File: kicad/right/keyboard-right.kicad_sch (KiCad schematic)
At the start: 87 parts, among them J1 Conn_01x04_Pin, J2 AudioJack4, J3 Conn_01x04_Pin, J4 Conn_01x04_Pin, J5 Conn_01x02_Pin, SW1 SW_Push, SW10 SW_Push, SW11 SW_Push, SW12 SW_Push, SW13 SW_Push, SW14 SW_Push, SW15 SW_Push, SW16 SW_Push, SW17 SW_Push, SW18 SW_Push, SW19 SW_Push, SW2 SW_Push, SW20 SW_Push, SW21 SW_Push, SW22 SW_Push, SW23 SW_Push, SW24 SW_Push, SW25 SW_Push, SW26 SW_Push, SW27 SW_Push, SW28 SW_Push, SW29 SW_Push, SW3 SW_Push, SW30 SW_Push, SW31 SW_Push, SW32 SW_Push, SW33 SW_Push, SW34 SW_Push, SW35 SW_Push, SW36 SW_Push, SW4 SW_Push, SW5 SW_Push, SW6 SW_Push, SW7 SW_Push, SW8 SW_Push, SW9 SW_Push, U1 AVR32DA32x-xPT

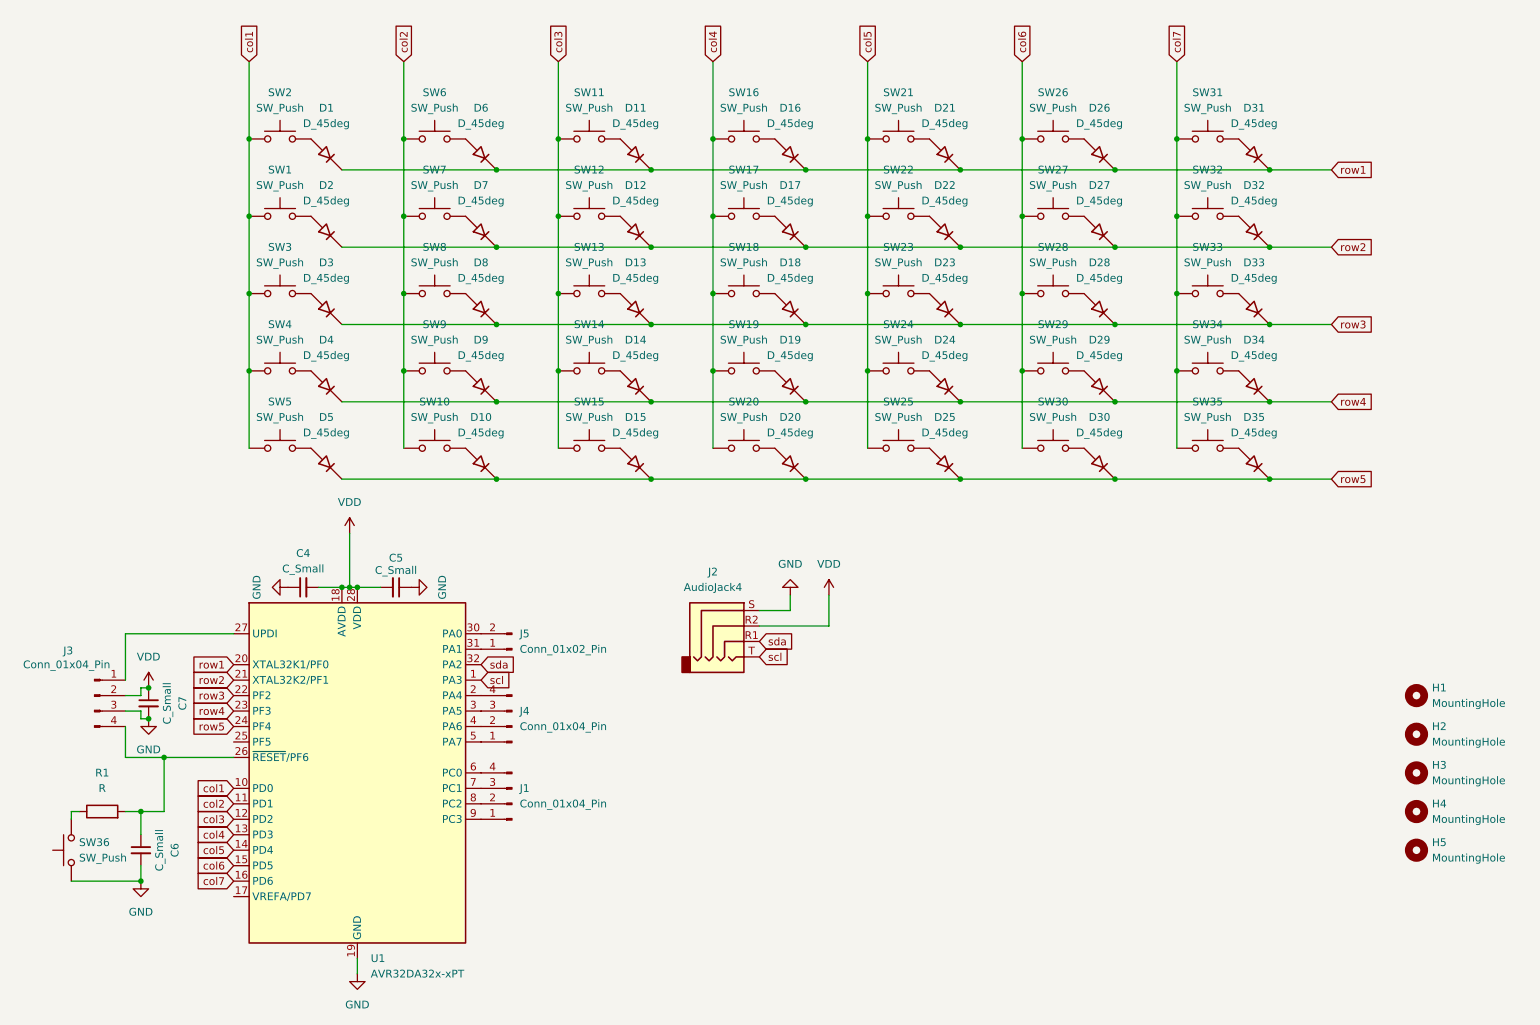
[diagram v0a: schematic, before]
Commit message: finished up right side pcb
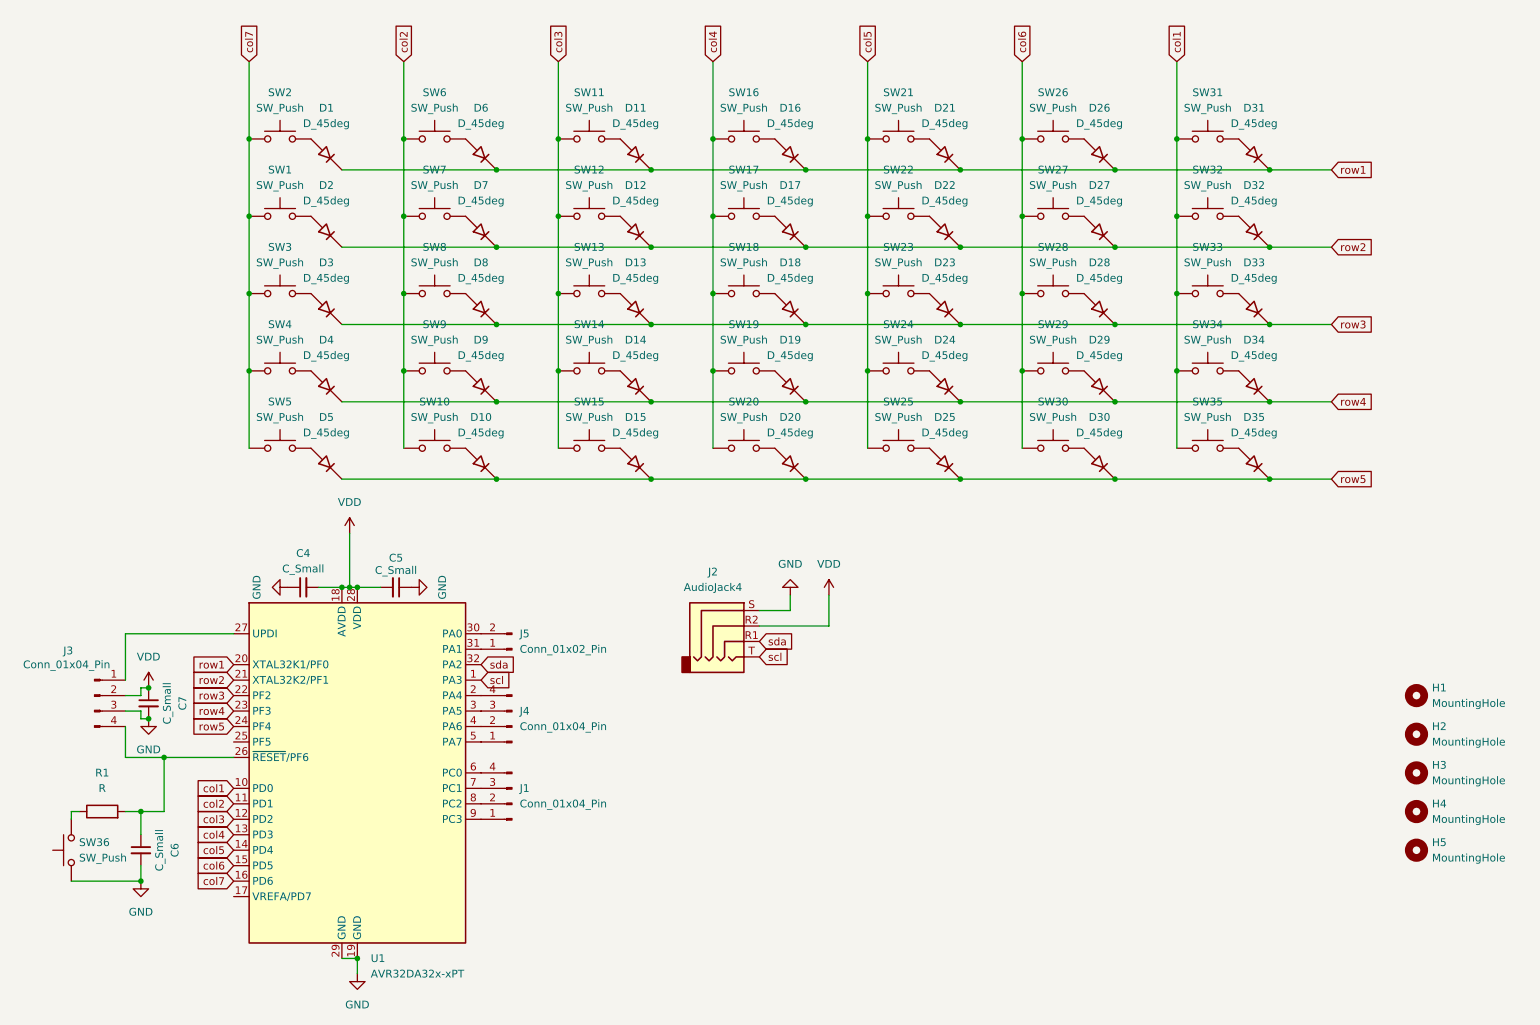
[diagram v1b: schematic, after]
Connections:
- net GND: now also U1.29 (GND)
- net col1: now also SW31.1, SW32.1, SW33.1, SW34.1, SW35.1; no longer SW1.1, SW2.1, SW3.1, SW4.1, SW5.1
- net col7: now also SW1.1, SW2.1, SW3.1, SW4.1, SW5.1; no longer SW31.1, SW32.1, SW33.1, SW34.1, SW35.1
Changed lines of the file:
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@@
+	)
+	(junction
+		(at 68.58 172.72)
+		(diameter 0)
+		(color 0 0 0 0)
 	)
 	(junction
@@
 	(wire
 		(pts
+			(xy 66.04 172.72) (xy 68.58 172.72)
+		)
+		(stroke
+			(width 0)
+			(type default)
+		)
+	)
+	(wire
+		(pts
 			(xy 218.44 68.58) (xy 228.6 68.58)
 		)
@@
 		)
 	)
+	(global_label "col7"
+		(shape input)
+		(at 50.8 25.4 90)
+		(fields_autoplaced yes)
+		(effects
+			(font
+				(size 1.27 1.27)
+			)
+			(justify left)
+		)
+		(property "Intersheetrefs" "${INTERSHEET_REFS}"
+			(at 50.8 18.3025 90)
+			(effects
+				(font
+					(size 1.27 1.27)
+				)
+				(justify left)
+				(hide yes)
+			)
+		)
+	)
+	(global_label "sda"
+		(shape input)
+		(at 134.62 120.65 0)
+		(fields_autoplaced yes)
+		(effects
+			(font
+				(size 1.27 1.27)
+			)
+			(justify left)
+		)
+		(property "Intersheetrefs" "${INTERSHEET_REFS}"
+			(at 140.9313 120.65 0)
+			(effects
+				(font
+					(size 1.27 1.27)
+				)
+				(justify left)
+				(hide yes)
+			)
+		)
+	)
+	(global_label "row3"
+		(shape input)
+		(at 228.6 68.58 0)
+		(fields_autoplaced yes)
+		(effects
+			(font
+				(size 1.27 1.27)
+			)
+			(justify left)
+		)
+		(property "Intersheetrefs" "${INTERSHEET_REFS}"
+			(at 236.0604 68.58 0)
+			(effects
+				(font
+					(size 1.27 1.27)
+				)
+				(justify left)
+				(hide yes)
+			)
+		)
+	)
+	(global_label "col6"
+		(shape input)
+		(at 177.8 25.4 90)
+		(fields_autoplaced yes)
+		(effects
+			(font
+				(size 1.27 1.27)
+			)
+			(justify left)
+		)
+		(property "Intersheetrefs" "${INTERSHEET_REFS}"
+			(at 177.8 18.3025 90)
+			(effects
+				(font
+					(size 1.27 1.27)
+				)
+				(justify left)
+				(hide yes)
+			)
+		)
+	)
+	(global_label "row1"
+		(shape input)
+		(at 48.26 124.46 180)
+		(fields_autoplaced yes)
+		(effects
+			(font
+				(size 1.27 1.27)
+			)
+			(justify right)
+		)
+		(property "Intersheetrefs" "${INTERSHEET_REFS}"
+			(at 40.7996 124.46 0)
+			(effects
+				(font
+					(size 1.27 1.27)
+				)
+				(justify right)
+				(hide yes)
+			)
+		)
+	)
+	(global_label "row3"
+		(shape input)
+		(at 48.26 129.54 180)
+		(fields_autoplaced yes)
+		(effects
+			(font
+				(size 1.27 1.27)
+			)
+			(justify right)
+		)
+		(property "Intersheetrefs" "${INTERSHEET_REFS}"
+			(at 40.7996 129.54 0)
+			(effects
+				(font
+					(size 1.27 1.27)
+				)
+				(justify right)
+				(hide yes)
+			)
+		)
+	)
+	(global_label "col3"
+		(shape input)
+		(at 101.6 25.4 90)
+		(fields_autoplaced yes)
+		(effects
+			(font
+				(size 1.27 1.27)
+			)
+			(justify left)
+		)
+		(property "Intersheetrefs" "${INTERSHEET_REFS}"
+			(at 101.6 18.3025 90)
+			(effects
+				(font
+					(size 1.27 1.27)
+				)
+				(justify left)
+				(hide yes)
+			)
+		)
+	)
+	(global_label "col2"
+		(shape input)
+		(at 48.26 147.32 180)
+		(fields_autoplaced yes)
+		(effects
+			(font
+				(size 1.27 1.27)
+			)
+			(justify right)
+		)
+		(property "Intersheetrefs" "${INTERSHEET_REFS}"
+			(at 41.1625 147.32 0)
+			(effects
+				(font
+					(size 1.27 1.27)
+				)
+				(justify right)
+				(hide yes)
+			)
+		)
+	)
+	(global_label "scl"
+		(shape input)
+		(at 134.62 123.19 0)
+		(fields_autoplaced yes)
+		(effects
+			(font
+				(size 1.27 1.27)
+			)
+			(justify left)
+		)
+		(property "Intersheetrefs" "${INTERSHEET_REFS}"
+			(at 140.3871 123.19 0)
+			(effects
+				(font
+					(size 1.27 1.27)
+				)
+				(justify left)
+				(hide yes)
+			)
+		)
+	)
+	(global_label "row5"
+		(shape input)
+		(at 228.6 93.98 0)
+		(fields_autoplaced yes)
+		(effects
+			(font
+				(size 1.27 1.27)
+			)
+			(justify left)
+		)
+		(property "Intersheetrefs" "${INTERSHEET_REFS}"
+			(at 236.0604 93.98 0)
+			(effects
+				(font
+					(size 1.27 1.27)
+				)
+				(justify left)
+				(hide yes)
+			)
+		)
+	)
 	(global_label "col1"
 		(shape input)
-		(at 50.8 25.4 90)
-		(fields_autoplaced yes)
-		(effects
-			(font
-				(size 1.27 1.27)
-			)
-			(justify left)
-		)
-		(property "Intersheetrefs" "${INTERSHEET_REFS}"
-			(at 50.8 18.3025 90)
-			(effects
-				(font
-					(size 1.27 1.27)
-				)
-				(justify left)
-				(hide yes)
-			)
-		)
-	)
-	(global_label "sda"
-		(shape input)
-		(at 134.62 120.65 0)
-		(fields_autoplaced yes)
-		(effects
-			(font
-				(size 1.27 1.27)
-			)
-			(justify left)
-		)
-		(property "Intersheetrefs" "${INTERSHEET_REFS}"
-			(at 140.9313 120.65 0)
-			(effects
-				(font
-					(size 1.27 1.27)
-				)
-				(justify left)
-				(hide yes)
-			)
-		)
-	)
-	(global_label "row3"
-		(shape input)
-		(at 228.6 68.58 0)
-		(fields_autoplaced yes)
-		(effects
-			(font
-				(size 1.27 1.27)
-			)
-			(justify left)
-		)
-		(property "Intersheetrefs" "${INTERSHEET_REFS}"
-			(at 236.0604 68.58 0)
-			(effects
-				(font
-					(size 1.27 1.27)
-				)
-				(justify left)
-				(hide yes)
-			)
-		)
-	)
-	(global_label "col6"
-		(shape input)
-		(at 177.8 25.4 90)
-		(fields_autoplaced yes)
-		(effects
-			(font
-				(size 1.27 1.27)
-			)
-			(justify left)
-		)
-		(property "Intersheetrefs" "${INTERSHEET_REFS}"
-			(at 177.8 18.3025 90)
-			(effects
-				(font
-					(size 1.27 1.27)
-				)
-				(justify left)
-				(hide yes)
-			)
-		)
-	)
-	(global_label "row1"
-		(shape input)
-		(at 48.26 124.46 180)
-		(fields_autoplaced yes)
-		(effects
-			(font
-				(size 1.27 1.27)
-			)
-			(justify right)
-		)
-		(property "Intersheetrefs" "${INTERSHEET_REFS}"
-			(at 40.7996 124.46 0)
-			(effects
-				(font
-					(size 1.27 1.27)
-				)
-				(justify right)
-				(hide yes)
-			)
-		)
-	)
-	(global_label "row3"
-		(shape input)
-		(at 48.26 129.54 180)
-		(fields_autoplaced yes)
-		(effects
-			(font
-				(size 1.27 1.27)
-			)
-			(justify right)
-		)
-		(property "Intersheetrefs" "${INTERSHEET_REFS}"
-			(at 40.7996 129.54 0)
-			(effects
-				(font
-					(size 1.27 1.27)
-				)
-				(justify right)
-				(hide yes)
-			)
-		)
-	)
-	(global_label "col3"
-		(shape input)
-		(at 101.6 25.4 90)
-		(fields_autoplaced yes)
-		(effects
-			(font
-				(size 1.27 1.27)
-			)
-			(justify left)
-		)
-		(property "Intersheetrefs" "${INTERSHEET_REFS}"
-			(at 101.6 18.3025 90)
-			(effects
-				(font
-					(size 1.27 1.27)
-				)
-				(justify left)
-				(hide yes)
-			)
-		)
-	)
-	(global_label "col2"
-		(shape input)
-		(at 48.26 147.32 180)
-		(fields_autoplaced yes)
-		(effects
-			(font
-				(size 1.27 1.27)
-			)
-			(justify right)
-		)
-		(property "Intersheetrefs" "${INTERSHEET_REFS}"
-			(at 41.1625 147.32 0)
-			(effects
-				(font
-					(size 1.27 1.27)
-				)
-				(justify right)
-				(hide yes)
-			)
-		)
-	)
-	(global_label "scl"
-		(shape input)
-		(at 134.62 123.19 0)
-		(fields_autoplaced yes)
-		(effects
-			(font
-				(size 1.27 1.27)
-			)
-			(justify left)
-		)
-		(property "Intersheetrefs" "${INTERSHEET_REFS}"
-			(at 140.3871 123.19 0)
-			(effects
-				(font
-					(size 1.27 1.27)
-				)
-				(justify left)
-				(hide yes)
-			)
-		)
-	)
-	(global_label "row5"
-		(shape input)
-		(at 228.6 93.98 0)
-		(fields_autoplaced yes)
-		(effects
-			(font
-				(size 1.27 1.27)
-			)
-			(justify left)
-		)
-		(property "Intersheetrefs" "${INTERSHEET_REFS}"
-			(at 236.0604 93.98 0)
-			(effects
-				(font
-					(size 1.27 1.27)
-				)
-				(justify left)
-				(hide yes)
-			)
-		)
-	)
-	(global_label "col7"
-		(shape input)
 		(at 203.2 25.4 90)
